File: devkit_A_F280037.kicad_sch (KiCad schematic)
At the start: 4 parts, among them J1 DEVKIT_C2000_ROW_A, J2 DEVKIT_C2000_ROW_B, J3 JTAG_CTBP_10, U1 TMS320F280037CSPM

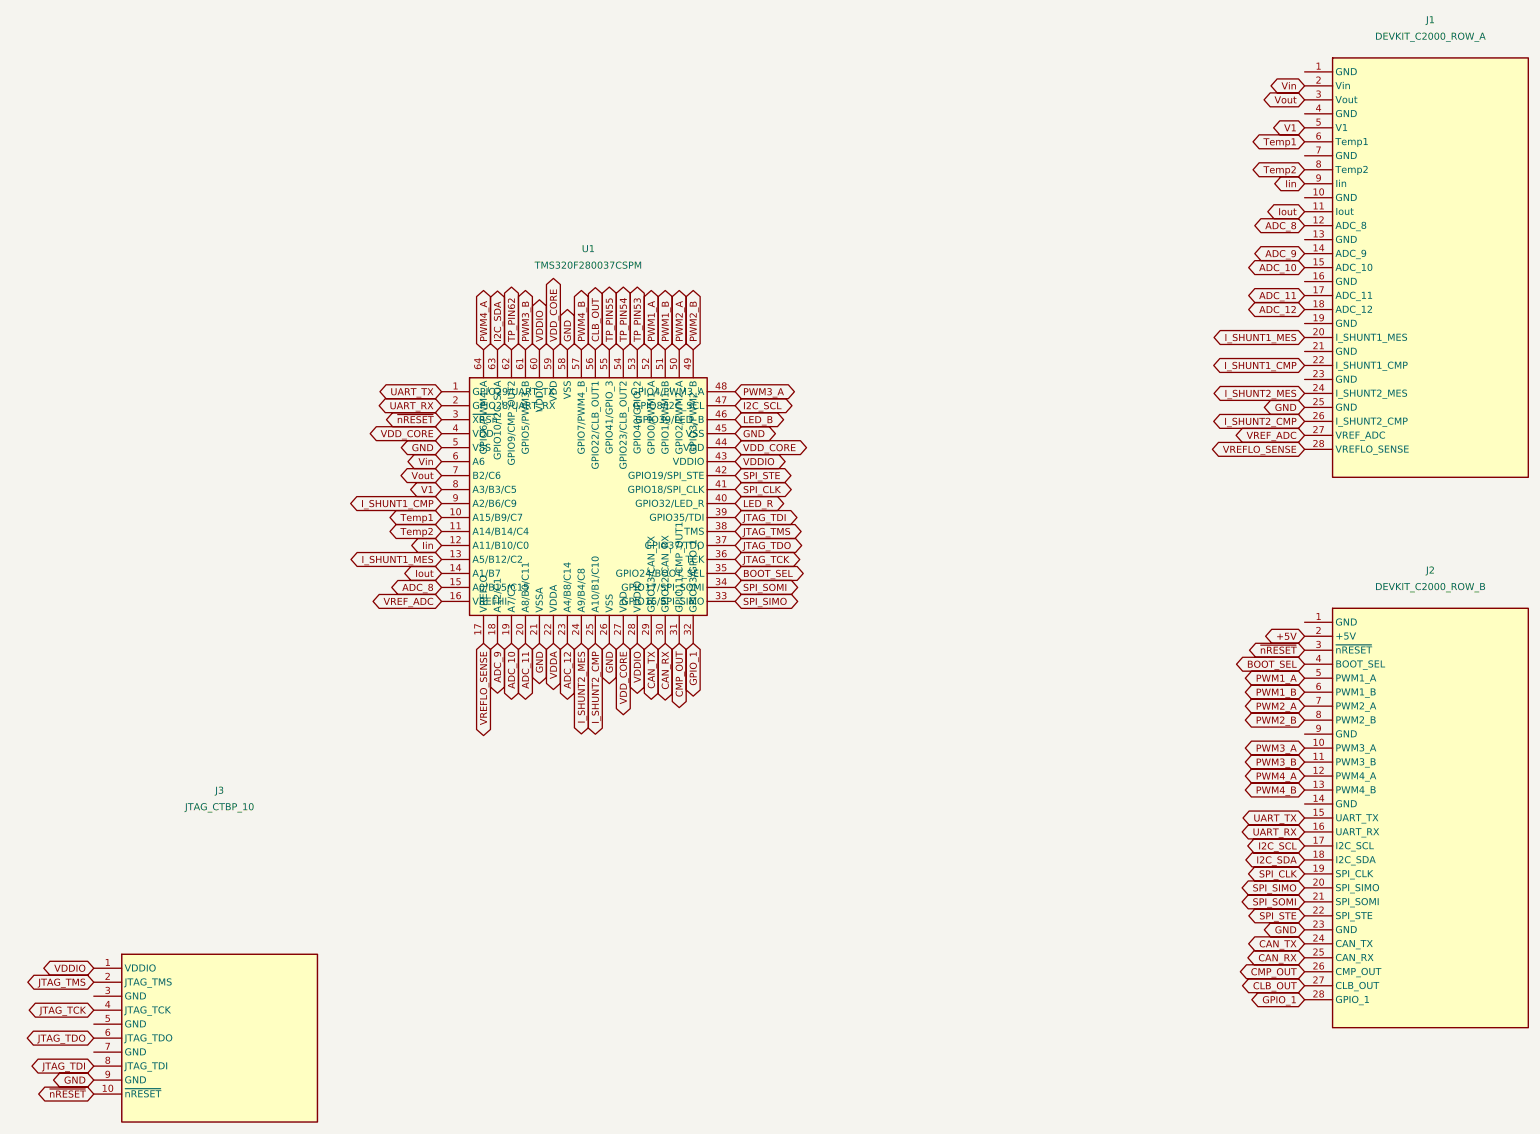
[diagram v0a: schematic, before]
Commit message: Recale les quatre symboles des devkits sur la grille de 1,27 mm
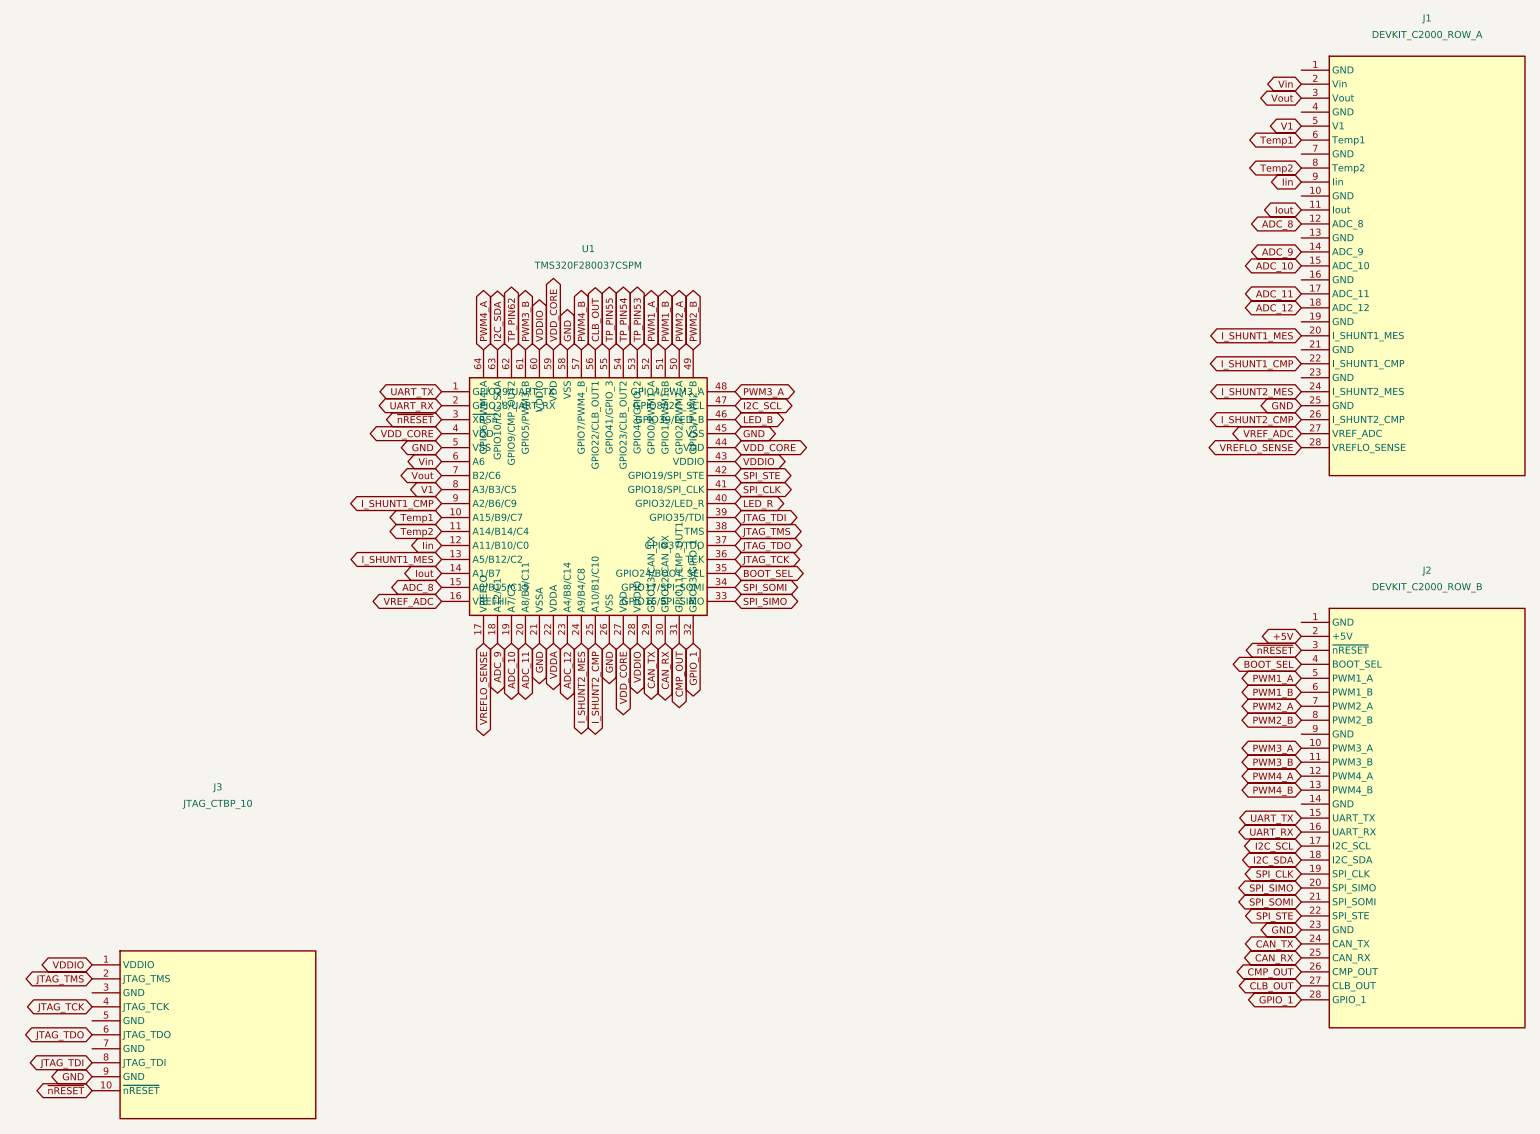
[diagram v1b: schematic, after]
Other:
- moved on the sheet: J1, J2, J3
